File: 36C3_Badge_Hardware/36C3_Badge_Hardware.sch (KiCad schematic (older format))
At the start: 157 parts, among them J1 MicroUSB, J2 ISP, Q1 FS8205A, Q10 MMBTA42, Q2 MMBTA42, Q3 MMBTA42, Q4 MMBTA92, Q5 MMBTA42, Q6 MMBTA42, Q7 MMBTA42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

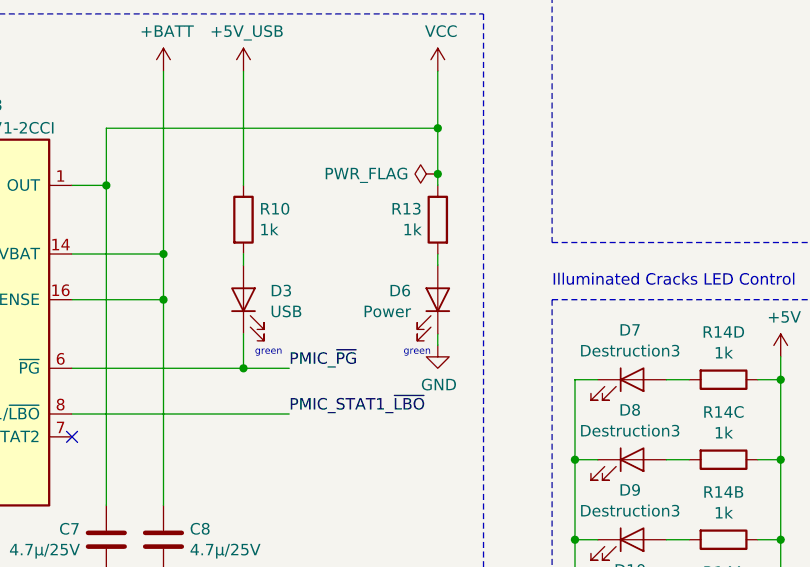
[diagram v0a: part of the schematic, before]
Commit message: Removed D6 (Power LED) since the switch is now gone too
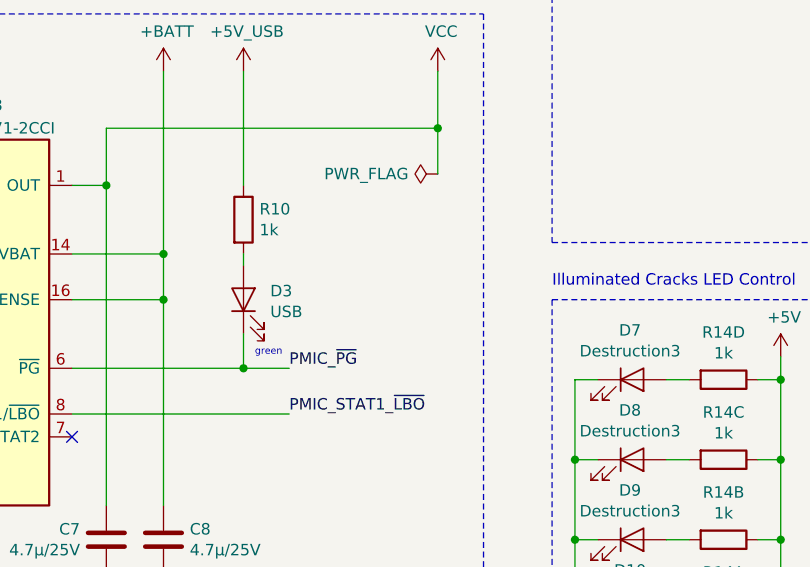
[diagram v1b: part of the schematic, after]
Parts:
- removed D6: Power, LEDs:LED_0603, symbol device:LED
- removed R13: 1k, Resistors_SMD:R_0603, symbol device:R
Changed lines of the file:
@@
 Wire Wire Line
 	4950 3400 4950 3900
-$Comp
-L device:LED D6
-U 1 1 60827B98
-P 5800 4400
-F 0 "D6" V 5838 4283 50  0000 R CNN
-F 1 "Power" V 5747 4283 50  0000 R CNN
-F 2 "LEDs:LED_0603" H 5800 4400 50  0001 C CNN
-F 3 "~" H 5800 4400 50  0001 C CNN
-	1    5800 4400
-	0    1    -1   0
-$EndComp
-$Comp
-L device:R R13
-U 1 1 60827B9E
-P 5800 4050
-F 0 "R13" H 5870 4096 50  0000 L CNN
-F 1 "1k" H 5870 4005 50  0000 L CNN
-F 2 "Resistors_SMD:R_0603" V 5730 4050 50  0001 C CNN
-F 3 "~" H 5800 4050 50  0001 C CNN
-	1    5800 4050
-	-1   0    0    -1
-$EndComp
-Wire Wire Line
-	5800 4200 5800 4250
-Text Notes 5650 4650 0    30   ~ 0
-green
-$Comp
-L power:GND #PWR026
-U 1 1 609D6125
-P 5800 4600
-F 0 "#PWR026" H 5800 4350 50  0001 C CNN
-F 1 "GND" H 5805 4427 50  0000 C CNN
-F 2 "" H 5800 4600 50  0001 C CNN
-F 3 "" H 5800 4600 50  0001 C CNN
-	1    5800 4600
-	1    0    0    -1
-$EndComp
-Wire Wire Line
-	5800 4550 5800 4600
 Wire Wire Line
 	15650 2500 15750 2500
@@
 	0    -1   -1   0
 $EndComp
-Connection ~ 5800 3850
-Wire Wire Line
-	5800 3850 5800 3900
 Wire Wire Line
 	4400 2100 4400 2200
